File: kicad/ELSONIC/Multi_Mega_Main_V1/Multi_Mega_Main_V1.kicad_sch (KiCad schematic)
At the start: 58 parts, among them J1 SMW250-04P, J2 Conn_ARM_SWD_10, J3 SMW250-03P, J4 SMW250-02P, J5 SMW250-04P, J7 Conn_01x03, J9 Conn_01x06, SW2 SW_Push, U1 STM32G474MET6, U2 UCC21520DW, U3 AMS1117-3.3, U4 74HCT574, U5 ULN2003, U6 74HCT574, Y1 HC-49SMD

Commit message: mcp 업데이트
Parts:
- added BZ1: Buzzer, symbol Device:Buzzer
- added C33, C34, C37, C38, C39, C40, C41: CL104K, 04_MyFoot_Passive:C_2012Metric, symbol 04_MyLib_Passive:C_Small
- added C35, C36: TAJB106K, 04_MyFoot_Passive:CP_EIA-3528-21_Kemet-B_HandSolder, symbol 04_MyLib_Passive:C_Pol
- added D2, D3, D4, D5, D6, D7: LED, symbol 03_MyLib_Active:LED
- added J10, J6: Conn_02x10_Odd_Even, symbol Connector_Generic:Conn_02x10_Odd_Even
- added J8: SMW250-04P, 02_MyFoot_Connectors:SMW250_04P, symbol 02_MyLib_Connectors:SMW250-04P
- added R10, R11, R12, R13, R8, R9: W8-J0561, 04_MyFoot_Passive:R_2012Metric, symbol 04_MyLib_Passive:R
- added R14, R15, R16, R17, R18: W8-J0103, 04_MyFoot_Passive:R_2012Metric, symbol 04_MyLib_Passive:R
- added R19: W4-J0220, 04_MyFoot_Passive:R_2012Metric, symbol 04_MyLib_Passive:R
- added TS1, TS2, TS3, TS4, TS5: TS1103D, symbol 06_MyLib_Mechanical:TS1103D
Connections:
- net +3.3V: now also C34.2, C36.1, J6.14 (Pin_14), J6.16 (Pin_16), J8.3, R14.2, R15.2, R16.2, R17.2, R18.2
- net +5V: now also C33.2, C35.1, J10.17 (Pin_17), J10.19 (Pin_19), J6.17 (Pin_17), J6.19 (Pin_19), J8.1, R19.2
- net CLK_LCD: now also J10.13 (Pin_13), J6.13 (Pin_13)
- net CLK_LED: now also J10.15 (Pin_15), J6.15 (Pin_15)
- net D0: now also J10.1 (Pin_1), J6.1 (Pin_1)
- net D1: now also J10.3 (Pin_3), J6.3 (Pin_3)
- net D2: now also J10.5 (Pin_5), J6.5 (Pin_5)
- net D3: now also J10.7 (Pin_7), J6.7 (Pin_7)
- net D4: now also J10.9 (Pin_9), J6.9 (Pin_9)
- net D5: now also J10.11 (Pin_11), J6.11 (Pin_11)
- net GND: now also C33.1, C34.1, C35.2, C36.2, C37.2, C38.2, C39.2, C40.2, C41.2, D2.1 (K), D3.1 (K), D4.1 (K), D5.1 (K), D6.1 (K), D7.1 (K), J10.18 (Pin_18), J10.20 (Pin_20), J6.18 (Pin_18), J6.20 (Pin_20), J8.2, J8.4, TS1.3, TS1.4, TS2.3, TS2.4, TS3.3, TS3.4, TS4.3, TS4.4, TS5.3, TS5.4
- net UP: now reaches U1.10 (PC2)
- net UP: now also C39.1, J10.6 (Pin_6), J6.6 (Pin_6), R16.1, TS3.1, TS3.2
- net DOWN: now reaches U1.11 (PC3)
- net DOWN: now also C40.1, J10.8 (Pin_8), J6.8 (Pin_8), R17.1, TS4.1, TS4.2
- net SET: now reaches U1.22 (PC4)
- net SET: now also C41.1, J10.10 (Pin_10), J6.10 (Pin_10), R18.1, TS5.1, TS5.2
- net BZ_OUT: now reaches U1.74 (PB5)
- net BZ_OUT: now also J10.12 (Pin_12), J6.12 (Pin_12)
- net START_STOP: now reaches U1.8 (PC0)
- net START_STOP: now also C37.1, J10.2 (Pin_2), J6.2 (Pin_2), R15.1, TS1.1, TS1.2
- net MODE: now reaches U1.9 (PC1)
- net MODE: now also C38.1, J10.4 (Pin_4), J6.4 (Pin_4), R14.1, TS2.1, TS2.2
- net at U6.14 (Q5): now also R13.2
- net at U6.15 (Q4): now also R8.2
- net at U6.16 (Q3): now also R9.2
- net at U6.17 (Q2): now also R10.2
- net at U6.18 (Q1): now also R11.2
- net at U6.19 (Q0): now also R12.2
- new net: D3.2 (A), R8.1
- new net: D5.2 (A), R10.1
- new net: D4.2 (A), R9.1
- new net: D6.2 (A), R11.1
- new net: BZ1.1 (+), R19.1
- new net: D2.2 (A), R13.1
- new net: D7.2 (A), R12.1
- new net: J10.14 (Pin_14), J10.16 (Pin_16)
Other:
- moved on the sheet: C31, U6

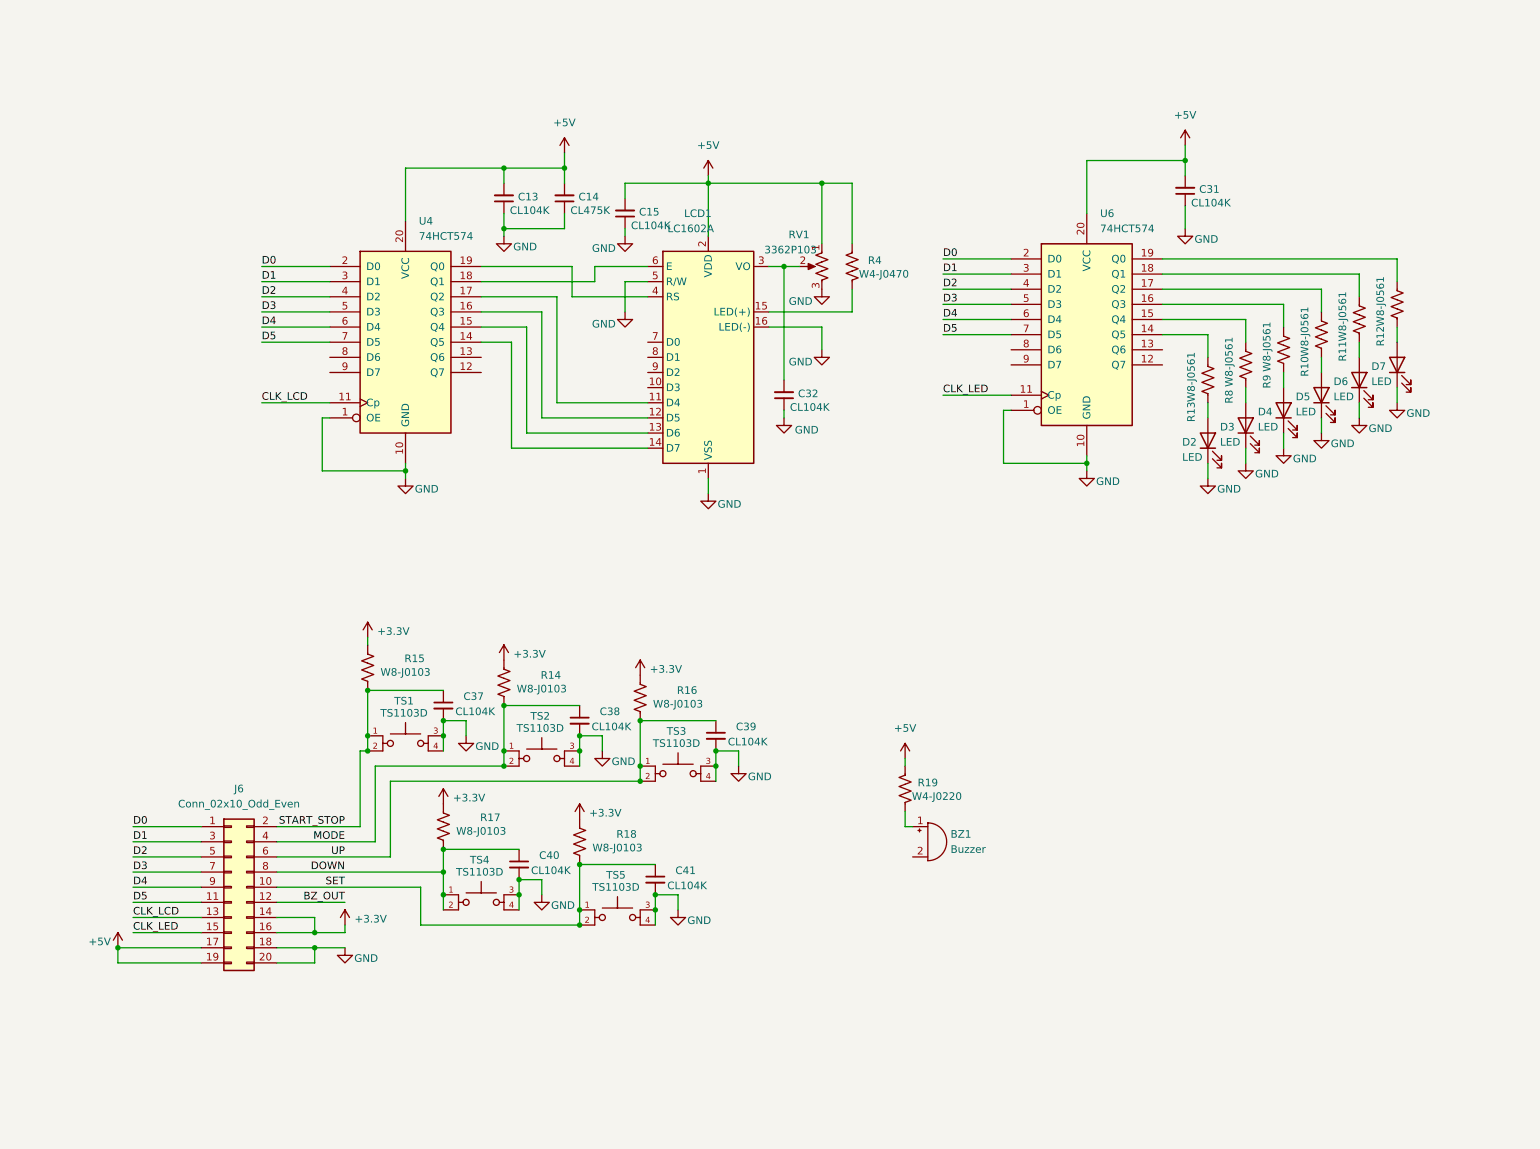
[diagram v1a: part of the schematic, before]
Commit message: kicad: update Multi_Mega_Main_V1, add SOT96P237X111-3N footprint, update MyLib_Active symbol
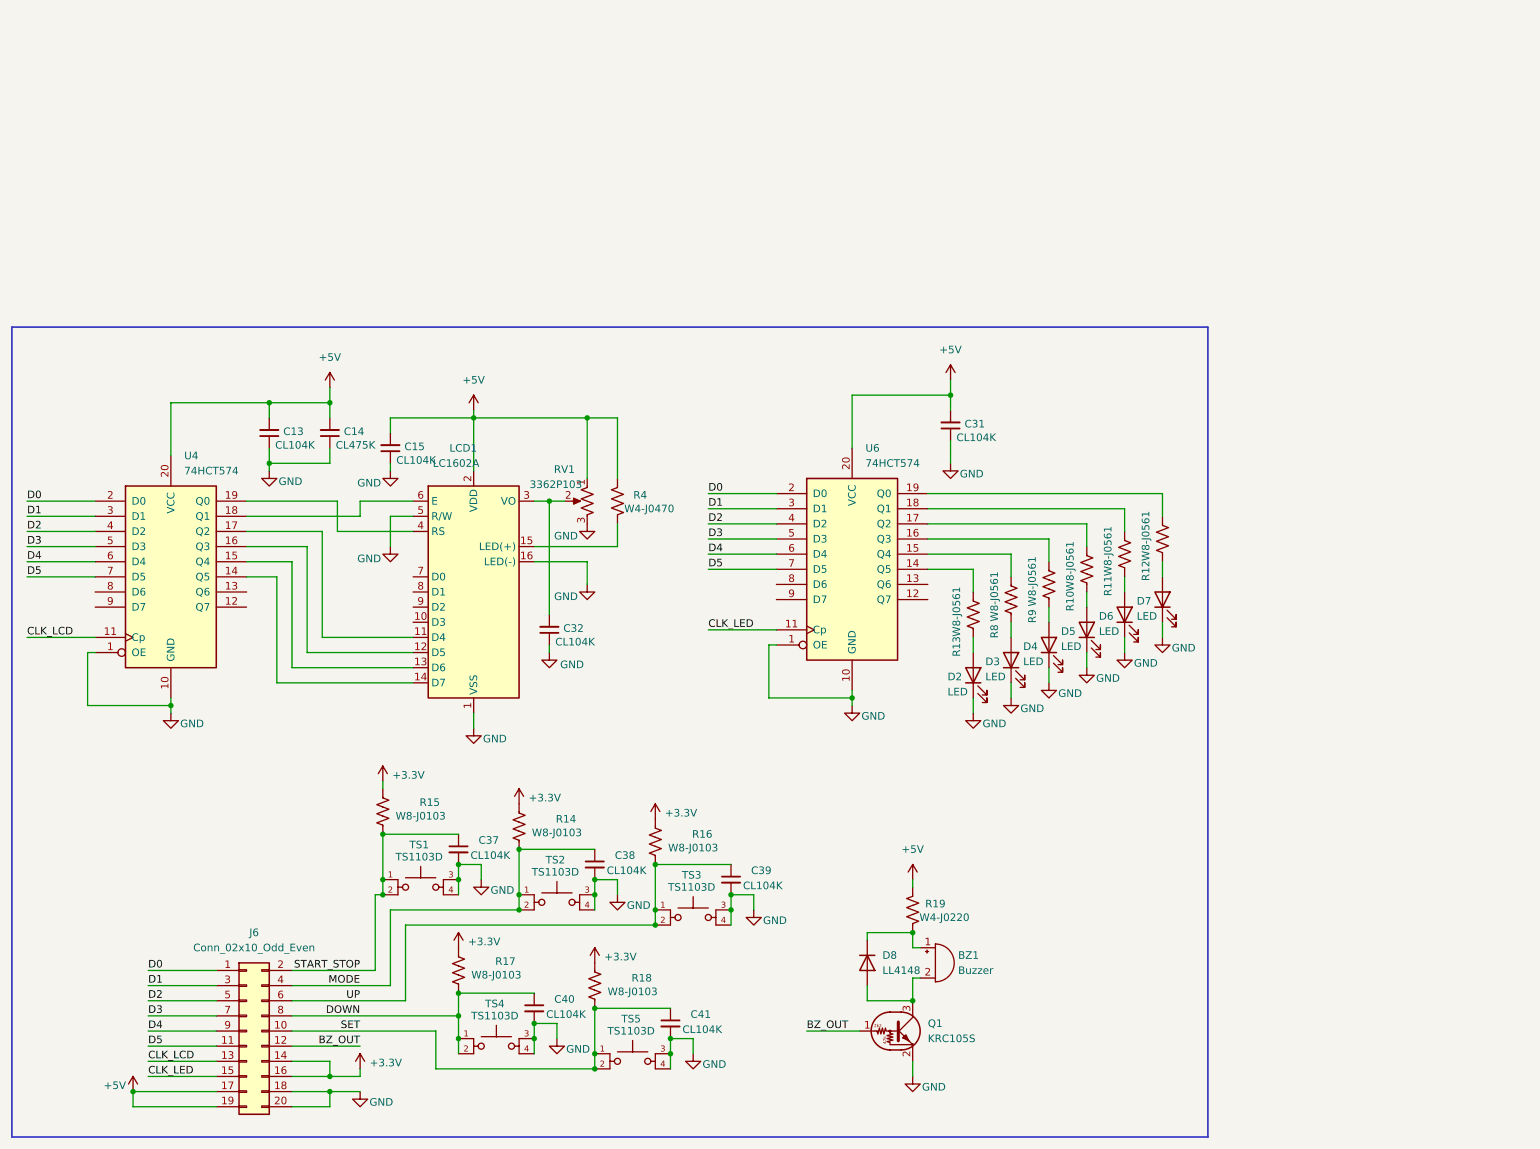
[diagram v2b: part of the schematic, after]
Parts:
- added D8: LL4148, symbol 03_MyLib_Active:LL4148
- added Q1: KRC105S, symbol 03_MyLib_Active:KRC105S
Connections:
- net BZ_OUT: now also Q1.1 (B)
- net GND: now also Q1.2 (E)
- net at BZ1.1 (+), R19.1: now also D8.1 (K)
- net at BZ1.2 (-): now also D8.2 (A), Q1.3 (C)
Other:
- moved on the sheet: BZ1, C13, C14, C15, C31, C32, C37, C38, C39, C40, C41, D2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

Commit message: 회로도 구성 완료
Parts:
- removed C17: TAJB107K, 04_MyFoot_Passive:CP_EIA-7343-31_Kemet-D_HandSolder, symbol 04_MyLib_Passive:C_Pol
- removed C35, C36: TAJB106K, 04_MyFoot_Passive:CP_EIA-3528-21_Kemet-B_HandSolder, symbol 04_MyLib_Passive:C_Pol
- removed J1, J5, J8: SMW250-04P, 02_MyFoot_Connectors:SMW250_04P, symbol 02_MyLib_Connectors:SMW250-04P
- removed J3: SMW250-03P, 02_MyFoot_Connectors:SMW250_03P, symbol 02_MyLib_Connectors:SMW250-03P
- removed J4: SMW250-02P, 02_MyFoot_Connectors:SMW250_02P, symbol 02_MyLib_Connectors:SMW250-02P
- removed J7: Conn_01x03, symbol Connector_Generic:Conn_01x03
- removed R5: W8-J0103, 04_MyFoot_Passive:R_2012Metric, symbol 04_MyLib_Passive:R
- removed R6: FR-0733RL, 04_MyFoot_Passive:R_2012Metric, symbol 04_MyLib_Passive:R
- removed U1: STM32G474MET6, 00_MyFoot_MCU:LQFP-80_12x12mm_P0.5mm, symbol MCU_ST_STM32G4:STM32G474METx
- removed U2: UCC21520DW, Package_SO:SOIC-16W_7.5x10.3mm_P1.27mm, symbol Driver_FET:UCC21520DW
- added C17: CL105K, 04_MyFoot_Passive:C_2012Metric, symbol 04_MyLib_Passive:C_Small
- added C35, C36, C77, C78, C79: B472K, 04_MyFoot_Passive:C_2012Metric, symbol 04_MyLib_Passive:C_Small
- added C42, C43: CG220J, 04_MyFoot_Passive:C_2012Metric, symbol 04_MyLib_Passive:C_Small
- added C44, C48, C50, C55, C68, C81, C83: CL104K, 04_MyFoot_Passive:C_2012Metric, symbol 04_MyLib_Passive:C_Small
- added C45, C56: TAJB106K, 04_MyFoot_Passive:CP_EIA-3528-21_Kemet-B_HandSolder, symbol 04_MyLib_Passive:C_Pol
- added C46, C47: 225J100V, 04_MyFoot_Passive:C_3216Metric, symbol 04_MyLib_Passive:C
- added C49: 47UF50V, 04_MyFoot_Passive:CP_EIA-3528-21_Kemet-B_HandSolder, symbol 04_MyLib_Passive:C_Pol
- added C51: 10UF25V, 04_MyFoot_Passive:CP_EIA-3528-21_Kemet-B_HandSolder, symbol 04_MyLib_Passive:C_Pol
- added C52: 104KC100V, 04_MyFoot_Passive:C_2012Metric, symbol 04_MyLib_Passive:C_Small
- added C53: 10UF100V, 04_MyFoot_Passive:CP_EIA-3528-21_Kemet-B_HandSolder, symbol 04_MyLib_Passive:C_Pol
- added C54: 1000UF63V, 04_MyFoot_Passive:CP_EIA-3528-21_Kemet-B_HandSolder, symbol 04_MyLib_Passive:C_Pol
- added C57: 105J100V, 04_MyFoot_Passive:C_3216Metric, symbol 04_MyLib_Passive:C
- added C58, C59: 0.1uF/100V, symbol 04_MyLib_Passive:C
- added C60: 1uF/100V, symbol 04_MyLib_Passive:C
- added C61: 102J100V, 04_MyFoot_Passive:C_3216Metric, symbol 04_MyLib_Passive:C
- added C62: 223J100V, 04_MyFoot_Passive:C_3216Metric, symbol 04_MyLib_Passive:C
- added C63, C65: 330J100V, 04_MyFoot_Passive:C_3216Metric, symbol 04_MyLib_Passive:C
- added C64: 220UF50V, 04_MyFoot_Passive:CP_EIA-3528-21_Kemet-B_HandSolder, symbol 04_MyLib_Passive:C_Pol
- added C66, C69: 103J100V, 04_MyFoot_Passive:C_3216Metric, symbol 04_MyLib_Passive:C
- added C67: 226J50V, 04_MyFoot_Passive:C_3216Metric, symbol 04_MyLib_Passive:C
- added C70: 101J100V, 04_MyFoot_Passive:C_3216Metric, symbol 04_MyLib_Passive:C
- added C71, C72: 10pF, symbol 04_MyLib_Passive:C
- added C73, C74, C75, C76: 100nF, symbol 04_MyLib_Passive:C
- added C80, C82: CL106K, 04_MyFoot_Passive:C_2012Metric, symbol 04_MyLib_Passive:C_Small
- added CT2: CT_TR, symbol 04_MyLib_Passive:CT_TROID
- added D10, D9: SS24, Diode_SMD:D_SMA, symbol Diode:SS24
- added D11: B3100-13-F, 03_MyFoot_Active:B3100_13_F, symbol 03_MyLib_Active:B3100-13-F
- added D12, D13: BAT54WS, Diode_SMD:D_SOD-323, symbol Diode:RF01VM2S
- added D14: SM712_SOT23, Package_TO_SOT_SMD:SOT-23, symbol Diode:SM712_SOT23
- added D15, D16, D17, D18, D19, D20, D21, D22, D23: LL4148, 03_MyFoot_Active:D_MELF_Hand, symbol 03_MyLib_Active:LL4148
- added DCDC1, DCDC2: MUS2415N, Converter_DCDC:Converter_DCDC_TRACO_TME_24xxS_Single_THT, symbol Converter_DCDC:TME-2415S
- added FC1, FC2: 470uF/63V, symbol 04_MyLib_Passive:C_Pol
- added IC1: LM5005MHX_NOPB, SOP65P640X110-21N, symbol 01_MyLib_ICs:LM5005MHX_NOPB
- added J1: Conn_01x02, symbol Connector_Generic:Conn_01x02
- added J12: Conn_01x04, symbol Connector_Generic:Conn_01x04
- added J3, J7: SMW250-02P, SMW25002, symbol 02_MyLib_Connectors:SMW250-02P
- added J4: Conn_02x13_Top_Bottom, symbol Connector_Generic:Conn_02x13_Top_Bottom
- added J5: Conn_01x03, symbol Connector_Generic:Conn_01x03
- added J8: Conn_ARM_JTAG_SWD_20, symbol Connector:Conn_ARM_JTAG_SWD_20
- added K1, K2, K3, K4, K5: PA1A_5V, 06_MyFoot_Mechanical:PA1A5V, symbol 06_MyLib_Mechanical:PA1A_5V
- added K6, K7, K8, K9: G6A274, 06_MyFoot_Mechanical:G6A274PST15USDC12, symbol 06_MyLib_Mechanical:G6A274
- added L1: Inductor, symbol 04_MyLib_Passive:Inductor
- added L2: 3.3uH, symbol 04_MyLib_Passive:Inductor
- added L3: 1.5uH, symbol 04_MyLib_Passive:Inductor
- added L4: 2.7uH, symbol 04_MyLib_Passive:Inductor
- added L5: 4.7uH, symbol 04_MyLib_Passive:Inductor
- added L6: 6.8uH, symbol 04_MyLib_Passive:Inductor
- added L7: 3.9uH, symbol 04_MyLib_Passive:Inductor
- added L8: 2.2uH, symbol 04_MyLib_Passive:Inductor
- added Q2, Q3: STD25N10F7, Package_TO_SOT_SMD:TO-252-2, symbol Transistor_FET:STD7NK40Z
- added R20, R53, R55, R57, R59, R61, R63: W8-J0103, 04_MyFoot_Passive:R_2012Metric, symbol 04_MyLib_Passive:R
- added R21: W8-J0104, 04_MyFoot_Passive:R_2012Metric, symbol 04_MyLib_Passive:R
- added R22, R25: W4-J0103, 04_MyFoot_Passive:R_2012Metric, symbol 04_MyLib_Passive:R
- added R23, R24: 1W-4.7, 04_MyFoot_Passive:R_2012Metric, symbol 04_MyLib_Passive:R
- added R26: W4-J0334, 04_MyFoot_Passive:R_2012Metric, symbol 04_MyLib_Passive:R
- added R27: W4-F4992, 04_MyFoot_Passive:R_2012Metric, symbol 04_MyLib_Passive:R
- added R28: W4-J0333, 04_MyFoot_Passive:R_2012Metric, symbol 04_MyLib_Passive:R
- added R29, R30: 15K/3W, symbol 04_MyLib_Passive:R
- added R31: 22K/3W, symbol 04_MyLib_Passive:R
- added R32, R39: W4-F1102, 04_MyFoot_Passive:R_2012Metric, symbol 04_MyLib_Passive:R
- added R33, R40: W4-F1501, 04_MyFoot_Passive:R_2012Metric, symbol 04_MyLib_Passive:R
- added R34: W4-F2701, 04_MyFoot_Passive:R_2012Metric, symbol 04_MyLib_Passive:R
- added R35: 1W-F100, Resistor_SMD:R_2512_6332Metric_Pad1.40x3.35mm_HandSolder, symbol 04_MyLib_Passive:R
- added R36: W4-J0100, 04_MyFoot_Passive:R_2012Metric, symbol 04_MyLib_Passive:R
- added R37: W4-J0123, 04_MyFoot_Passive:R_2012Metric, symbol 04_MyLib_Passive:R
- added R38: W4-J0223, 04_MyFoot_Passive:R_2012Metric, symbol 04_MyLib_Passive:R
- added R41, R42, R43, R44, R45, R46: 200, symbol 04_MyLib_Passive:R
- added R47, R48: 10K, symbol 04_MyLib_Passive:R
- added R49, R50: W8-J0431, 04_MyFoot_Passive:R_2012Metric, symbol 04_MyLib_Passive:R
- added R51: W4-J0121, 04_MyFoot_Passive:R_2012Metric, symbol 04_MyLib_Passive:R
- added R52, R54, R56, R58, R60: W4-J0472, 04_MyFoot_Passive:R_3216Metric, symbol 04_MyLib_Passive:R
- added R62: FR-0733RL, 04_MyFoot_Passive:R_2012Metric, symbol 04_MyLib_Passive:R
- added SW1: SW_DIP_x02, symbol Switch:SW_DIP_x02
- added T2: OUTPUT_Transformer, symbol 04_MyLib_Passive:Transformer_1P_1S
- added U1: STM32G474RBT6, Package_QFP:LQFP-64_10x10mm_P0.5mm, symbol 00_MyLib_MCU:STM32G474RBT6
- added U10, U11, U12, U13, U9: TLP185, 01_MyFoot_ICs:SOIC-4_4.55x3.7mm_P2.54mm, symbol Isolator:TLP185
- added U14: ULN2003, symbol 01_MyLib_ICs:ULN2003
- added U2: UCC21520DW, Package_SO:SOIC-16W_7.5x10.3mm_P1.27mm, symbol 01_MyLib_ICs:UCC21520DW
- added U7: MAX3485, Package_SO:SOIC-8_3.9x4.9mm_P1.27mm, symbol Interface_UART:MAX3485
- added U8: INA190A4, Package_TO_SOT_SMD:SOT-363_SC-70-6, symbol 01_MyLib_ICs:INA190A4
- C10: value TAJB106K -> 47UF50V
- C12: value TAJB106K -> 10UF25V
- C3: value CG220J -> CL104K
- C33: value CL104K -> CL105K
- C4: value CG220J -> CL475K
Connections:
- net +3.3V: now also C16.2, C3.2, C4.2, J10.14 (Pin_14), J10.16 (Pin_16), C17.2, C55.2, C56.1, C68.2, J5.1 (Pin_1), R49.2, R53.2, R55.2, R57.2, R59.2, R61.2, U1.1 (VBAT), U1.16 (VDD), U1.32 (VDD), U1.48 (VDD), U1.64 (VDD), U2.3 (VCCI), U2.8, U7.8 (VCC), U8.3 (V+); no longer C10.1, C34.2, C9.2
- net +5V: now also U5.9 (COM), C44.2, C45.1, C80.2, C81.2, C82.2, C83.2, D15.1 (K), D16.1 (K), D17.1 (K), D18.1 (K), D19.1 (K), D20.1 (K), D21.1 (K), D22.1 (K), D23.1 (K), J12.3 (Pin_3), K1.2 (++), K2.2 (++), K3.2 (++), K4.2 (++), K5.2 (++), K6.1 (COIL+), K7.1 (COIL+), K8.1 (COIL+), K9.1 (COIL+), U14.9 (COM); no longer C11.2, C12.1, C16.2, C33.2
- net BZ_OUT: now also U1.23 (PC5)
- net CLK_LCD: now also U1.3 (PC14)
- net CLK_LED: now also U1.4 (PC15)
- net D0: now also U1.30 (PB10)
- net D1: now also U1.33 (PB11)
- net D2: now also U1.34 (PB12)
- net D3: now also U1.35 (PB13)
- net D4: now also U1.36 (PB14)
- net D5: now also U1.37 (PB15)
- net DOWN: now also U1.11 (PC3)
- net GND: now also J2.9 (GNDDetect), U5.8 (GND), C17.1, C35.1, C36.1, C42.1, C43.1, C44.1, C45.2, C48.1, C49.2, C55.1, C56.2, C71.1, C72.1, C75.1, C76.1, C77.1, C78.1, C79.1, C80.1, C81.1, C82.1, C83.1, DCDC1.1 (-Vin), DCDC2.1 (-Vin), J12.2 (Pin_2), J12.4 (Pin_4), J4.25 (Pin_25), J4.9 (Pin_9), J5.3 (Pin_3), J7.2, R20.1, R21.1, R41.1, R42.1, R47.1, R48.1, R50.1, R63.1, U1.15 (VSS), U1.27 (VSSA), U1.31 (VSS), U1.47 (VSS), U1.63 (VSS), U10.4, U11.4, U12.4, U13.4, U14.8 (GND), U2.4 (GND), U7.5 (GND), U9.4; no longer C11.1, C12.2
- net INA: now also R1.2, C42.2, U2.1 (INA); no longer C3.2
- net INB: now also R2.2, C43.2, U2.2 (INB); no longer C4.2
- net MODE: now also U1.9 (PC1)
- net NRST: now also U1.7 (PG10)
- net SET: now also U1.22 (PC4)
- net START_STOP: now also U1.8 (PC0)
- net SWCLK: now also U1.50 (PA14)
- net SWDIO: now also U1.49 (PA13)
- net UP: now also U1.10 (PC2)
- net USART1_RX: now also U1.60 (PB7)
- net USART1_TX: now also R62.2
- net at C2.2, Y1.1: now also U1.6 (PF1)
- net at C27.2, C28.2, C29.2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: now also U1.28 (VREF+), U1.29 (VDDA)
- net at C1.2, Y1.2: now also U1.5 (PF0)
- net CHA1: now reaches R1.1
- net CHA1: now also U1.42 (PA8)
- net CHA2: now reaches R2.1
- net CHA2: now also U1.43 (PA9)
- net LOW_ALARM: now reaches U5.1 (I1)
- net LOW_ALARM: now also U1.44 (PA10)
- net at U5.12 (O5): now also D19.2 (A), K5.1 (-)
- net at U5.13 (O4): now also D18.2 (A), K4.1 (-)
- net at U5.14 (O3): now also D17.2 (A), K3.1 (-)
- net at U5.15 (O2): now also D16.2 (A), K2.1 (-)
- net at U5.16 (O1): now also D15.2 (A), K1.1 (-)
- net GOING: now reaches U5.2 (I2)
- net GOING: now also U1.45 (PA11)
- net HIGH_ALARM: now reaches U5.3 (I3)
- net HIGH_ALARM: now also U1.56 (PB3)
- net TD_ALARM: now reaches U5.4 (I4)
- net TD_ALARM: now also U1.57 (PB4)
- net TOTAL_ALARM: now reaches U5.5 (I5)
- net TOTAL_ALARM: now also U1.46 (PA12)
- new net: D23.2 (A), K9.16 (COIL-), U14.13 (O4)
- new net: D22.2 (A), K8.16 (COIL-), U14.14 (O3)
- new net: D21.2 (A), K7.16 (COIL-), U14.15 (O2)
- new net: D20.2 (A), K6.16 (COIL-), U14.16 (O1)
- new net: D14.1 (A1), D14.2 (A2), J3.1, R49.1, SW1.3, U7.6 (A)
- new net: D14.3 (common), J3.2, R50.2, SW1.4, U7.7 (B)
- new net: K8.11 (NC2), K8.6 (NC1), K9.13 (COM2), K9.4 (COM1), L5.2, L6.1
- new net: K7.11 (NC2), K7.6 (NC1), K8.13 (COM2), K8.4 (COM1), L4.2, L5.1
- new net: C74.1, D13.2 (A)
- new net: C74.2, R45.1, R46.1
- new net: C66.1, C69.2, IC1.7 (FB), R32.1, R33.2, R34.1, R38.1
- new net: D10.2 (A), Q3.1 (G), R24.1, R25.2
- new net: C71.2, CT2.4, L2.1, L7.1
- new net: D10.1 (K), R24.2, U2.10 (OUTB)
- new net: C64.1, C67.2, IC1.12 (OUT), L1.2, R32.2, R35.2, R39.2, U8.4 (+)
- new net: CT2.1, R41.2, R43.2, R44.2
- new net: CT2.2, R42.2, R45.2, R46.2
- new net: C72.2, CT2.3, T2.4 (SB)
- new net: D9.1 (K), R23.2, U2.15 (OUTA)
- new net: D9.2 (A), Q2.1 (G), R22.2, R23.1
- new net: C61.2, IC1.11 (SS)
- new net: J5.2 (Pin_2), R63.2, U1.61 (PB8)
- new net: C73.1, D12.2 (A)
- new net: C73.2, R43.1, R44.1
- new net: C66.2, R27.1
- new net: R51.1, SW1.1
- new net: R51.2, SW1.2
- new net: R54.1, U10.1
- new net: R60.1, U13.1
- new net: C58.1, C59.2, FC1.2, FC2.1, R29.1, R30.2, T2.2 (AB)
- new net: C70.2, IC1.6 (COMP), R27.2, R38.2
- new net: R52.1, U9.1
- new net: R21.2, U2.6 (DT)
- new net: IC1.2 (SD), R26.2, R37.1
- new net: C57.2, IC1.1 (VCC)
- new net: C65.2, IC1.9 (RAMP)
- new net: C63.1, R36.2
- new net: C62.1, C63.2, D11.1 (K), IC1.17 (SW_1), IC1.18 (SW_2), IC1.19 (PRE), L1.1
- new net: K6.11 (NC2), K6.6 (NC1), K7.13 (COM2), K7.4 (COM1), L3.2, L4.1, L8.2
- new net: J8.10 (GND), J8.12 (GND), J8.14 (GND), J8.16 (GND), J8.18 (GND), J8.20 (GND), J8.4 (GND), J8.6 (GND), J8.8 (GND)
- new net: R56.1, U11.1
- new net: IC1.8 (RT), R28.2
- new net: R20.2, U2.5 (DIS)
- new net: R58.1, U12.1
- new net: C62.2, IC1.20 (BST)
- new net: R62.1, U1.59 (PB6)
- new net: D11.2 (A), IC1.15 (IS_1), IC1.16 (IS_2)
- new net +15VA: C11.2, C12.1, DCDC1.4 (+Vout), U2.16 (VDDA)
- new net +15VB: C50.2, C51.1, DCDC2.4 (+Vout), Q2.3 (S), Q3.2 (D), R22.1, T2.1 (AA), U2.11 (VDDB)
- new net +24V: C10.1, C33.2, C34.2, C48.2, C49.1, C9.2, DCDC1.2 (+Vin), DCDC2.2 (+Vin), J12.1 (Pin_1), R52.2, R54.2, R56.2, R58.2, R60.2
- new net +48V: C46.2, C47.2, C52.2, C53.1, C54.1, IC1.3 (VIN_1), IC1.4 (VIN_2), J1.1 (Pin_1), R26.1
- new net +VBUS: C58.2, C60.2, FC1.1, Q2.2 (D), R29.2, R31.2, R35.1, U8.5 (-)
- new net ADC1_IN1: C75.2, D12.1 (K), R47.2, U1.12 (PA0)
- new net ADC1_IN2: C76.2, D13.1 (K), R48.2, U1.13 (PA1)
- new net ADC2_IN3: U1.20 (PA6), U8.6
- new net ADC2_IN4: R39.1, R40.2, U1.21 (PA7)
- new net BCD_BIT1: J4.11 (Pin_11), U10.3
- new net BCD_BIT1_M: C36.2, R55.1, U1.52 (PC10), U10.6
- new net BCD_BIT2: J4.23 (Pin_23), U11.3
- new net BCD_BIT2_M: C77.2, R57.1, U1.53 (PC11), U11.6
- new net BCD_BIT3: J4.10 (Pin_10), U12.3
- new net BCD_BIT3_M: C78.2, R59.1, U1.54 (PC12), U12.6
- new net DAC1_OUT1: R34.2, U1.18 (PA4)
- new net DE_RS485: U1.24 (PB0), U7.3 (DE)
- new net GNDA: C11.1, C12.2, DCDC1.3 (-Vout), U2.14 (VSSA)
- new net GNDB: C46.1, C47.1, C50.1, C51.2, C52.1, C53.2, C54.2, C57.1, C59.1, C60.1, C61.1, C64.2, C65.1, C67.1, C68.1, C69.1, C70.1, DCDC2.3 (-Vout), FC2.2, IC1.10 (AGND), IC1.13 (PGND_1), IC1.14 (PGND_2), J1.2 (Pin_2), Q3.3 (S), R25.1, R28.1, R30.1, R31.1, R33.1, R36.1, R37.2, R40.1, U2.9 (VSSB), U8.1 (REF), U8.2 (GND)
- new net GNDPZT: T2.3 (SA)
- new net GOING_A: J4.2 (Pin_2), K2.5
- new net GOING_C: J4.15 (Pin_15), K2.6
- new net HIGH_ALARM_A: J4.3 (Pin_3), K3.5
- new net HIGH_ALARM_C: J4.16 (Pin_16), K3.6
- new net LC_REL1: U1.38 (PC6), U14.1 (I1)
- new net LC_REL2: U1.39 (PC7), U14.2 (I2)
- new net LC_REL3: U1.40 (PC8), U14.3 (I3)
- new net LC_REL4: U1.41 (PC9), U14.4 (I4)
- new net LC_RELAY_IN: K6.13 (COM2), K6.4 (COM1), L2.2, L3.1, L7.2, L8.1
- new net LC_RELAY_OUT: J7.1, K9.11 (NC2), K9.6 (NC1), L6.2
- new net LOW_ALARM_A: J4.1 (Pin_1), K1.5
- new net LOW_ALARM_C: J4.14 (Pin_14), K1.6
- new net REMOTE: J4.22 (Pin_22), U9.3
- new net REMOTE_M: C35.2, R53.1, U1.51 (PA15), U9.6
- new net SENSOR: J4.13 (Pin_13), U13.3
- new net SENSOR_M: C79.2, R61.1, U1.55 (PD2), U13.6
- new net TD_ALARM_A: J4.6 (Pin_6), K4.5
- new net TD_ALARM_C: J4.19 (Pin_19), K4.6
- new net TOTAL_ALARM_A: J4.7 (Pin_7), K5.5
- new net TOTAL_ALARM_C: J4.20 (Pin_20), K5.6
- new net USART2_RX: U1.17 (PA3), U7.1 (RO)
- new net USART2_TX: U1.14 (PA2), U7.4 (DI)
- new net /RE_RS485: U1.25 (PB1), U7.2 (~{RE})
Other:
- moved on the sheet: C1, C18, C19, C2, C20, C21, C22, C23, C24, C25, C26, C27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

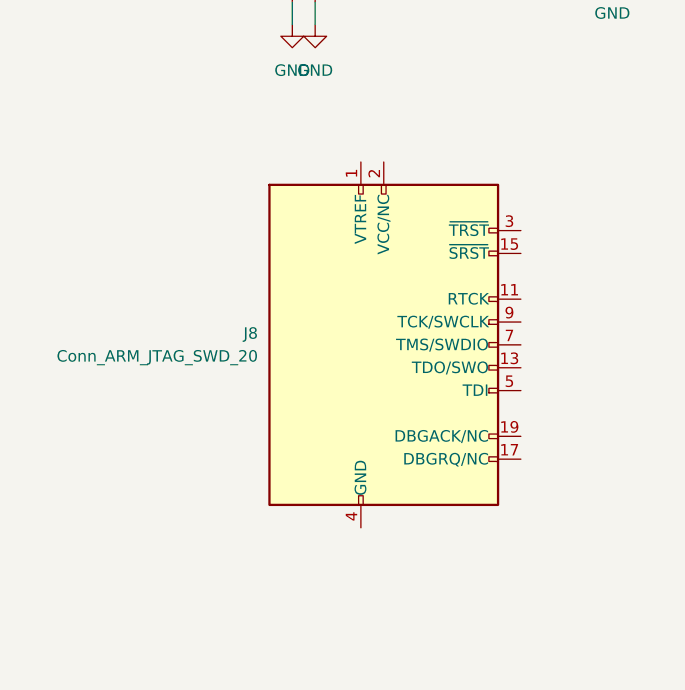
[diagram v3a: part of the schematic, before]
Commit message: chore: KiCad 아트웍 및 라이브러리 변경 반영
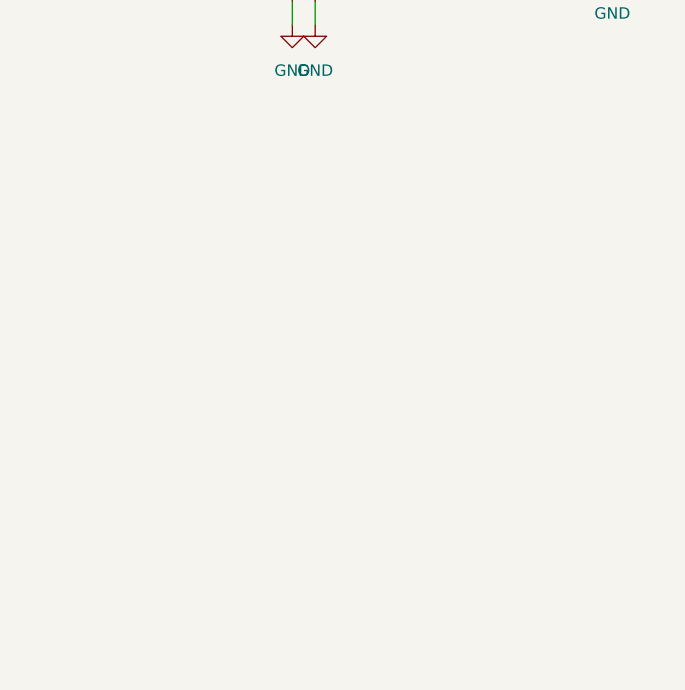
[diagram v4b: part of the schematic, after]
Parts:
- removed J8: Conn_ARM_JTAG_SWD_20, symbol Connector:Conn_ARM_JTAG_SWD_20
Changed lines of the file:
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@@
-	)
-	(symbol
-		(lib_id "Connector:Conn_ARM_JTAG_SWD_20")
-		(at 46.99 97.79 0)
-		(unit 1)
-		(exclude_from_sim no)
-		(in_bom yes)
-		(on_board yes)
-		(dnp no)
-		(fields_autoplaced yes)
-		(property "Reference" "J8"
-			(at 33.02 96.52 0)
-			(effects
-				(font
-					(size 1.27 1.27)
-				)
-				(justify right)
-			)
-		)
-		(property "Value" "Conn_ARM_JTAG_SWD_20"
-			(at 33.02 99.06 0)
-			(effects
-				(font
-					(size 1.27 1.27)
-				)
-				(justify right)
-			)
-		)
-		(property "Footprint" ""
-			(at 58.42 124.46 0)
-			(effects
-				(font
-					(size 1.27 1.27)
-				)
-				(justify left top)
-				(hide yes)
-			)
-		)
-		(property "Datasheet" "http://infocenter.arm.com/help/topic/com.arm.doc.dui0499b/DUI0499B_system_design_reference.pdf"
-			(at 38.1 129.54 90)
-			(effects
-				(font
-					(size 1.27 1.27)
-				)
-				(hide yes)
-			)
-		)
-		(property "Description" "Standard IDC20 Pinheader Connector, ARM legacy JTAG and SWD interface"
-			(at 46.99 97.79 0)
-			(effects
-				(font
-					(size 1.27 1.27)
-				)
-				(hide yes)
-			)
-		)
-		(pin "16"
-		)
-		(pin "1"
-		)
-		(pin "10"
-		)
-		(pin "4"
-		)
-		(pin "12"
-		)
-		(pin "14"
-		)
-		(pin "18"
-		)
-		(pin "20"
-		)
-		(pin "8"
-		)
-		(pin "5"
-		)
-		(pin "15"
-		)
-		(pin "17"
-		)
-		(pin "19"
-		)
-		(pin "2"
-		)
-		(pin "3"
-		)
-		(pin "9"
-		)
-		(pin "6"
-		)
-		(pin "11"
-		)
-		(pin "7"
-		)
-		(pin "13"
-		)
-		(instances
-			(project ""
-				(path "/a17ba0bf-4277-4371-85c8-23d9e5782086"
-					(reference "J8")
-					(unit 1)
-				)
-			)
-		)
 	)
 	(symbol
